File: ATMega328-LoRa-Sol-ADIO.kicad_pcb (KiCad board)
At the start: 2 copper layers, 93 x 61 mm, 48 parts, among them J1 USB_B_Micro, J2 External Power, J3 AIO/I2C, J4 Solar, J5 RXTX+Power, J6 SMA, J7 Conn_01x06, Q1 IRLML5203, U1 AP1117-33, U2 CH340G, U3 LP2985-3.3, U4 RFM95W-868S2, U5 SPV1040TTR, U6 ATmega328P-A, U7 DS3231M, Y1 12MHz, Y2 8MHz

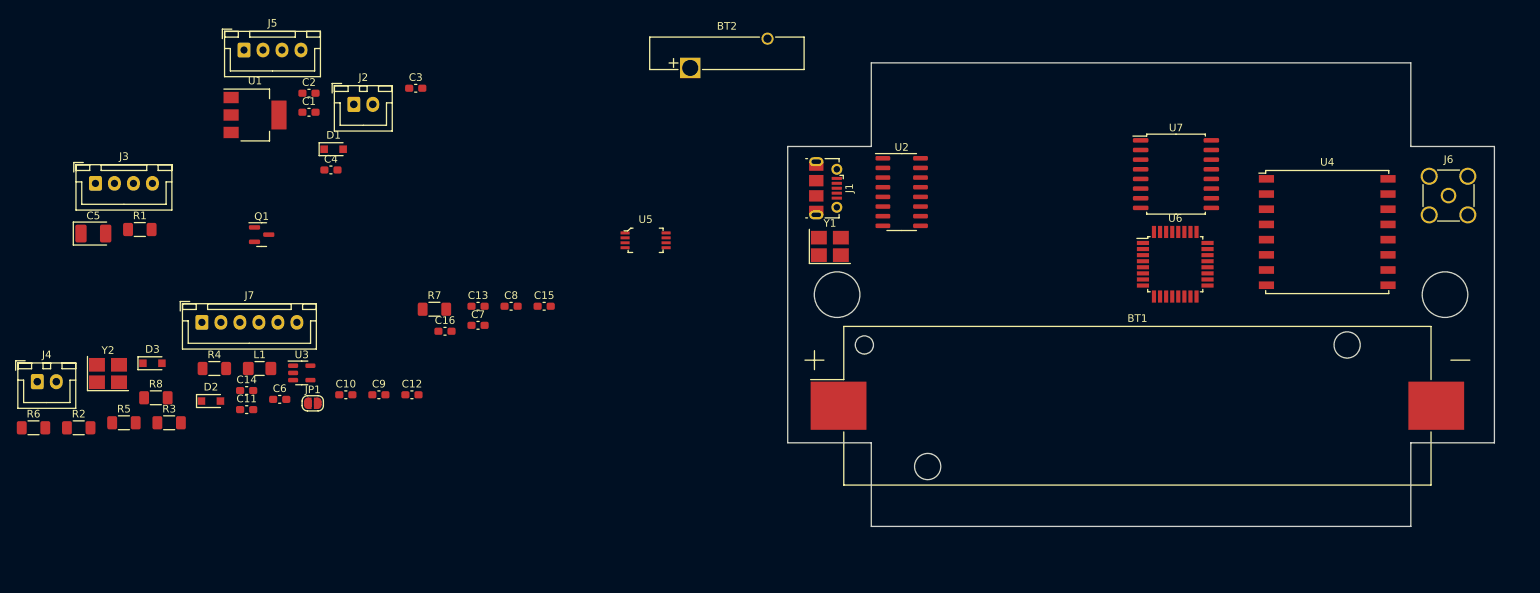
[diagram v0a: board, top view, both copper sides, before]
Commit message: Further work on the ATMega328 PCB
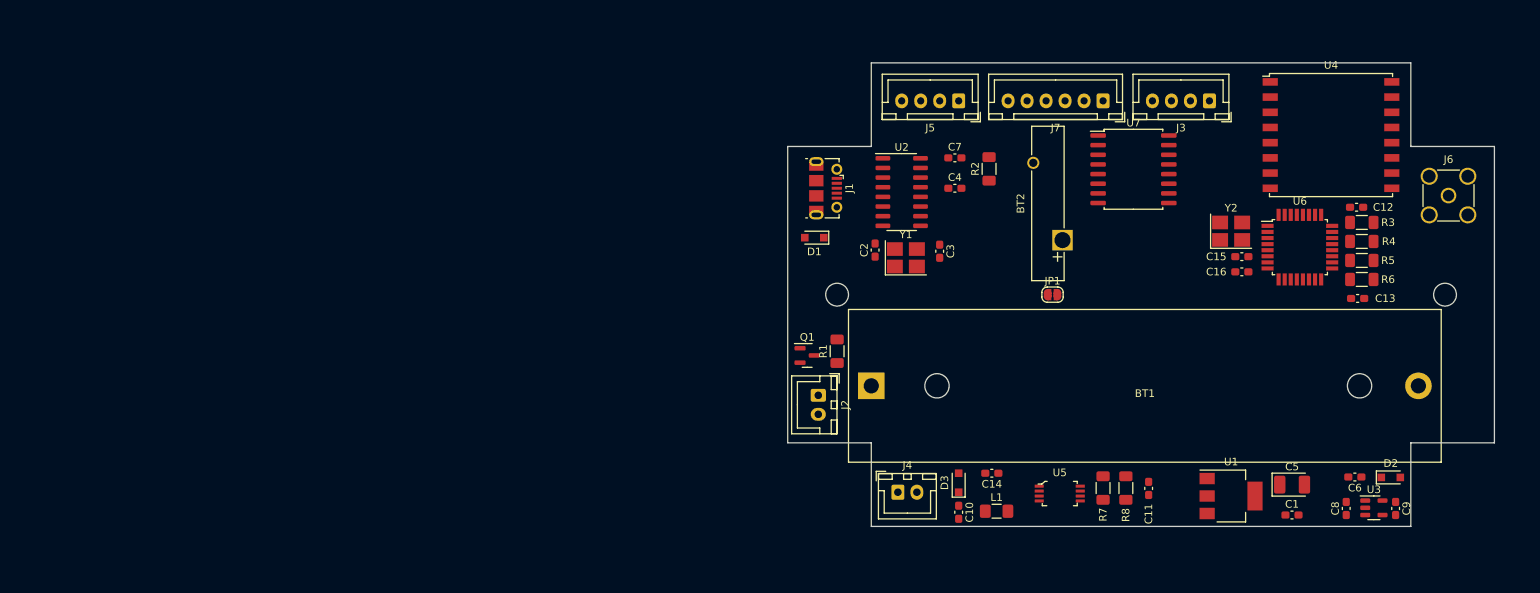
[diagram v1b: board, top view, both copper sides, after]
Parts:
- BT1: footprint Battery:BatteryHolder_Keystone_1042_1x18650 -> Battery:BatteryHolder_MPD_BH-18650-PC2
- moved R6 175.9 mm to (189.6, 54.5)
- moved R5 164.3 mm to (189.6, 52.0), turned to 180 degrees
- moved C5 161.2 mm to (180.4, 81.5)
- moved R3 159.1 mm to (189.6, 47.0), turned to 180 degrees
- moved D2 155.6 mm to (193.4, 80.5)
- moved R4 151.9 mm to (189.6, 49.5)
- moved Y2 149.0 mm to (172.3, 48.1)
- moved J3 147.0 mm to (169.5, 31.0), turned to 180 degrees
- moved U3 142.2 mm to (191.1, 84.5)
- moved C6 141.9 mm to (188.6, 80.5), turned to 180 degrees
- moved C1 139.8 mm to (180.4, 85.5)
- moved U1 137.9 mm to (172.3, 83.0)
- moved C9 134.6 mm to (194.0, 84.6), turned to -90 degrees
- moved R8 128.2 mm to (158.5, 82.0), turned to 90 degrees
- moved C12 126.7 mm to (188.9, 45.0)
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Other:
- outline, holes or cut-outs redrawn

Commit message: Update the PCB Board and add nets to it
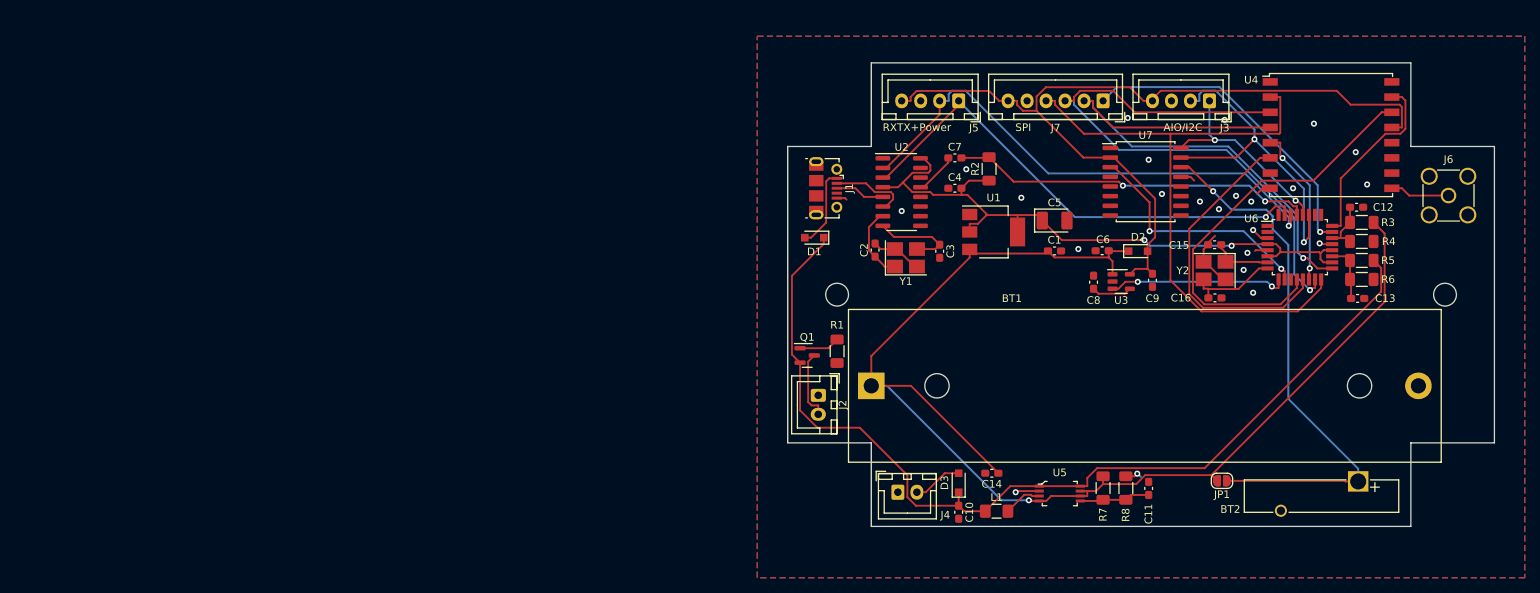
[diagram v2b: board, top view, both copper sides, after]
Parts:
- J7: value Conn_01x06 -> SPI
- moved BT2 50.2 mm to (189.1, 81.1), turned to 180 degrees
- moved C1 46.7 mm to (149.1, 50.8)
- moved C5 46.7 mm to (149.1, 46.8)
- moved U1 46.7 mm to (141.1, 48.2)
- moved C6 44.6 mm to (155.4, 50.7)
- moved C8 44.6 mm to (154.2, 54.9)
- moved D2 44.6 mm to (160.1, 50.8)
- moved U3 44.6 mm to (157.9, 54.8)
- moved C9 43.9 mm to (162.0, 54.6)
- moved JP1 33.1 mm to (171.2, 81.0), turned to 180 degrees
- moved Y2 5.63 mm to (170.2, 53.3), turned to 180 degrees
- moved C16 4.93 mm to (170.2, 56.9), turned to 0 degrees
- moved C15 3.91 mm to (170.2, 49.9)
- moved U7 2.29 mm to (161.1, 41.6)
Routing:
- net +BATT: track 0.00 -> 168.7 mm, vias 0 -> 1
- net +5V: track 0.00 -> 127.5 mm
- net +3.3VA: track 0.00 -> 110.4 mm
- net +3V3: track 0.00 -> 86.0 mm, vias 0 -> 2
- net Lora_MISO: track 0.00 -> 82.2 mm
- net Lora_MOSI: track 0.00 -> 78.1 mm, vias 0 -> 1
- net Net-(BT2-Pad1): track 0.00 -> 71.6 mm, vias 0 -> 1
- net Lora_SCK: track 0.00 -> 71.6 mm, vias 0 -> 1
- net RX: track 0.00 -> 68.8 mm, vias 0 -> 1
- net TX: track 0.00 -> 65.5 mm, vias 0 -> 1
- net Lora_DIO0: track 0.00 -> 55.7 mm
- net AT-RST: track 0.00 -> 48.0 mm, vias 0 -> 2
- net SDA: track 0.00 -> 43.7 mm, vias 0 -> 2
- net SPI_SS: track 0.00 -> 42.2 mm, vias 0 -> 1
- net Lora_RST: track 0.00 -> 41.0 mm
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- added copper zone on B.Cu, net Earth
- added copper zone on F.Cu, net Earth

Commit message: First set of gerber files for production
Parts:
- added D4: B5817WS-TP, Diode_SMD:D_SOD-323_HandSoldering, F.Cu at (138.8, 55.5)
- added JP2: Solar Powered, Jumper:SolderJumper-2_P1.3mm_Open_Pad1.0x1.5mm, F.Cu at (143.8, 55.6)
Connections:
- BT1 pad 1: +BATT -> Net-(BT1-Pad1)
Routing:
- net +BATT: track 168.7 -> 140.7 mm, vias 1 -> 2
- net Net-(BT1-Pad1): track 0.00 -> 23.8 mm
- net Earth: track 31.3 -> 24.8 mm, vias 23 -> 16
- net +3.3VA: track 110.4 -> 109.4 mm
- net TX: track 65.5 -> 64.6 mm
- net Net-(C12-Pad1): track 7.09 -> 6.46 mm
- net CLOCK_INT: track 31.9 -> 31.4 mm
